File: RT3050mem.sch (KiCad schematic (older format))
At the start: 17 parts, among them P3 CONN_1, U1 RT3050, U2 29LV320, U3 SDRAM54

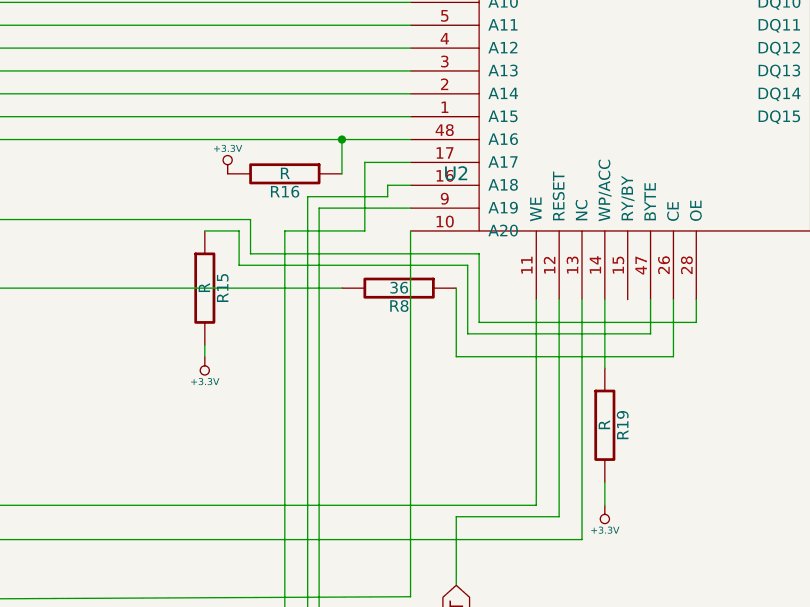
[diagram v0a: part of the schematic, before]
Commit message: updated component values
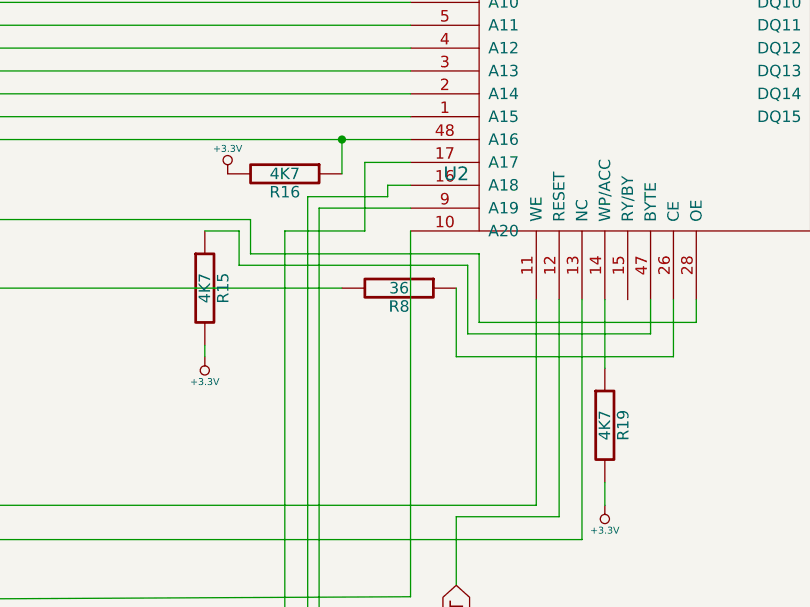
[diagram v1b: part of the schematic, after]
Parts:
- R15, R16, R19: value R -> 4K7
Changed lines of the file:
@@
-EESchema Schematic File Version 2  date Tue 02 Sep 2014 05:26:51 BST
+EESchema Schematic File Version 2
 LIBS:power
 LIBS:device
@@
 LIBS:AIC809
 LIBS:rt3050-cache
-EELAYER 25  0
+EELAYER 25 0
 EELAYER END
-$Descr A3 16535 11700
+$Descr A3 16535 11693
 encoding utf-8
 Sheet 4 6
@@
 F 0 "#PWR017" H 9850 550 30  0001 C CNN
 F 1 "GND" H 9850 480 30  0001 C CNN
+F 2 "" H 9850 550 60  0001 C CNN
+F 3 "" H 9850 550 60  0001 C CNN
 	1    9850 550
 	1    0    0    -1
@@
 F 0 "R18" V 9930 150 50  0000 C CNN
 F 1 "R" V 9850 150 50  0000 C CNN
+F 2 "" H 9850 150 60  0001 C CNN
+F 3 "" H 9850 150 60  0001 C CNN
 	1    9850 150
 	1    0    0    -1
@@
 F 0 "P3" H 1680 3100 40  0000 L CNN
 F 1 "CONN_1" H 1600 3155 30  0001 C CNN
+F 2 "" H 1600 3100 60  0001 C CNN
+F 3 "" H 1600 3100 60  0001 C CNN
 	1    1600 3100
 	-1   0    0    1
@@
 F 0 "#PWR018" H 10450 8350 30  0001 C CNN
 F 1 "GND" H 10450 8280 30  0001 C CNN
+F 2 "" H 10450 8350 60  0001 C CNN
+F 3 "" H 10450 8350 60  0001 C CNN
 	1    10450 8350
 	1    0    0    -1
@@
 F 0 "#PWR019" H 11350 8300 30  0001 C CNN
 F 1 "GND" H 11350 8230 30  0001 C CNN
+F 2 "" H 11350 8300 60  0001 C CNN
+F 3 "" H 11350 8300 60  0001 C CNN
 	1    11350 8300
 	1    0    0    -1
@@
 F 0 "C25" H 11000 8350 50  0000 L CNN
 F 1 "C" H 11000 8150 50  0000 L CNN
+F 2 "" H 10950 8250 60  0001 C CNN
+F 3 "" H 10950 8250 60  0001 C CNN
 	1    10950 8250
 	0    1    1    0
@@
 F 0 "#PWR020" H 10650 8210 30  0001 C CNN
 F 1 "+3.3V" H 10650 8360 30  0000 C CNN
+F 2 "" H 10650 8250 60  0001 C CNN
+F 3 "" H 10650 8250 60  0001 C CNN
 	1    10650 8250
 	1    0    0    -1
@@
 F 0 "#PWR021" H 10350 11960 30  0001 C CNN
 F 1 "+3.3V" H 10350 12110 30  0000 C CNN
+F 2 "" H 10350 12000 60  0001 C CNN
+F 3 "" H 10350 12000 60  0001 C CNN
 	1    10350 12000
 	-1   0    0    1
@@
 P 10350 11650
 F 0 "R19" V 10430 11650 50  0000 C CNN
-F 1 "R" V 10350 11650 50  0000 C CNN
+F 1 "4K7" V 10350 11650 50  0000 C CNN
+F 2 "" H 10350 11650 60  0001 C CNN
+F 3 "" H 10350 11650 60  0001 C CNN
 	1    10350 11650
 	1    0    0    -1
@@
 F 0 "#PWR022" H 8600 11310 30  0001 C CNN
 F 1 "+3.3V" H 8600 11460 30  0000 C CNN
+F 2 "" H 8600 11350 60  0001 C CNN
+F 3 "" H 8600 11350 60  0001 C CNN
 	1    8600 11350
 	-1   0    0    1
@@
 P 8600 11050
 F 0 "R15" V 8680 11050 50  0000 C CNN
-F 1 "R" V 8600 11050 50  0000 C CNN
+F 1 "4K7" V 8600 11050 50  0000 C CNN
+F 2 "" H 8600 11050 60  0001 C CNN
+F 3 "" H 8600 11050 60  0001 C CNN
 	1    8600 11050
 	1    0    0    -1
@@
 P 8950 10550
 F 0 "R16" V 9030 10550 50  0000 C CNN
-F 1 "R" V 8950 10550 50  0000 C CNN
+F 1 "4K7" V 8950 10550 50  0000 C CNN
+F 2 "" H 8950 10550 60  0001 C CNN
+F 3 "" H 8950 10550 60  0001 C CNN
 	1    8950 10550
 	0    1    1    0
@@
 F 0 "#PWR023" H 8700 10510 30  0001 C CNN
 F 1 "+3.3V" H 8700 10660 30  0000 C CNN
+F 2 "" H 8700 10550 60  0001 C CNN
+F 3 "" H 8700 10550 60  0001 C CNN
 	1    8700 10550
 	1    0    0    -1
@@
 F 0 "U2" H 9700 8150 60  0000 C CNN
 F 1 "29LV320" H 10100 10250 60  0000 C CNN
+F 2 "" H 10100 9350 60  0001 C CNN
+F 3 "" H 10100 9350 60  0001 C CNN
 	1    10100 9350
 	1    0    0    -1
@@
 F 0 "#PWR024" H 9550 260 30  0001 C CNN
 F 1 "+3.3V" H 9550 410 30  0000 C CNN
+F 2 "" H 9550 300 60  0001 C CNN
+F 3 "" H 9550 300 60  0001 C CNN
 	1    9550 300
 	1    0    0    -1
@@
 F 0 "R17" V 9630 600 50  0000 C CNN
 F 1 "R" V 9550 600 50  0000 C CNN
+F 2 "" H 9550 600 60  0001 C CNN
+F 3 "" H 9550 600 60  0001 C CNN
 	1    9550 600
 	1    0    0    -1
@@
 F 0 "R14" V 8430 3550 50  0000 C CNN
 F 1 "R" V 8350 3550 50  0000 C CNN
+F 2 "" H 8350 3550 60  0001 C CNN
+F 3 "" H 8350 3550 60  0001 C CNN
 	1    8350 3550
 	1    0    0    -1
@@
 F 0 "#PWR025" H 9100 1910 30  0001 C CNN
 F 1 "+3.3V" H 9100 2060 30  0000 C CNN
+F 2 "" H 9100 1950 60  0001 C CNN
+F 3 "" H 9100 1950 60  0001 C CNN
 	1    9100 1950
 	1    0    0    -1
@@
 F 0 "#PWR026" H 9500 3550 30  0001 C CNN
 F 1 "GND" H 9500 3480 30  0001 C CNN
+F 2 "" H 9500 3550 60  0001 C CNN
+F 3 "" H 9500 3550 60  0001 C CNN
 	1    9500 3550
 	1    0    0    -1
@@
 F 0 "R7" V 9030 1300 50  0000 C CNN
 F 1 "36" V 8950 1300 50  0000 C CNN
+F 2 "" H 8950 1300 60  0001 C CNN
+F 3 "" H 8950 1300 60  0001 C CNN
 	1    8950 1300
 	1    0    0    -1
@@
 F 0 "R8" V 9530 11050 50  0000 C CNN
 F 1 "36" V 9450 11050 50  0000 C CNN
+F 2 "" H 9450 11050 60  0001 C CNN
+F 3 "" H 9450 11050 60  0001 C CNN
 	1    9450 11050
 	0    1    1    0
@@
 F 0 "R6" V 8830 1300 50  0000 C CNN
 F 1 "36" V 8750 1300 50  0000 C CNN
+F 2 "" H 8750 1300 60  0001 C CNN
+F 3 "" H 8750 1300 60  0001 C CNN
 	1    8750 1300
 	1    0    0    -1
@@
 F 0 "R5" V 8680 1300 50  0000 C CNN
 F 1 "36" V 8600 1300 50  0000 C CNN
+F 2 "" H 8600 1300 60  0001 C CNN
+F 3 "" H 8600 1300 60  0001 C CNN
 	1    8600 1300
 	1    0    0    -1
@@
 F 0 "R4" V 8530 1300 50  0000 C CNN
 F 1 "100" V 8450 1300 50  0000 C CNN
+F 2 "" H 8450 1300 60  0001 C CNN
+F 3 "" H 8450 1300 60  0001 C CNN
 	1    8450 1300
 	1    0    0    -1
@@
 F 0 "R3" V 8380 1300 50  0000 C CNN
 F 1 "36" V 8300 1300 50  0000 C CNN
+F 2 "" H 8300 1300 60  0001 C CNN
+F 3 "" H 8300 1300 60  0001 C CNN
 	1    8300 1300
 	1    0    0    -1
@@
 F 0 "U3" H 10650 2700 60  0000 C CNN
 F 1 "SDRAM54" H 10650 -650 60  0000 C CNN
+F 2 "" H 10650 1650 60  0001 C CNN
+F 3 "" H 10650 1650 60  0001 C CNN
 	1    10650 1650
 	1    0    0    -1
@@
 F 0 "U1" H 5350 -1150 60  0000 C CNN
 F 1 "RT3050" H 5250 8200 60  0000 C CNN
+F 2 "" H 5350 4300 60  0001 C CNN
+F 3 "" H 5350 4300 60  0001 C CNN
 	2    5350 4300
 	1    0    0    -1
